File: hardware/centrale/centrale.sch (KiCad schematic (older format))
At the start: 36 parts, among them J1 MDCOG240128B6W, J2 Conn_BME280, J3 CONN_BME280_2, J4 RJ45, J5 Term_sel, Q1 BSS123, U1 MCP7940N-xSN, U2 TPS54228, U3 MCP2542FDxMF, Y1 32.768Khz

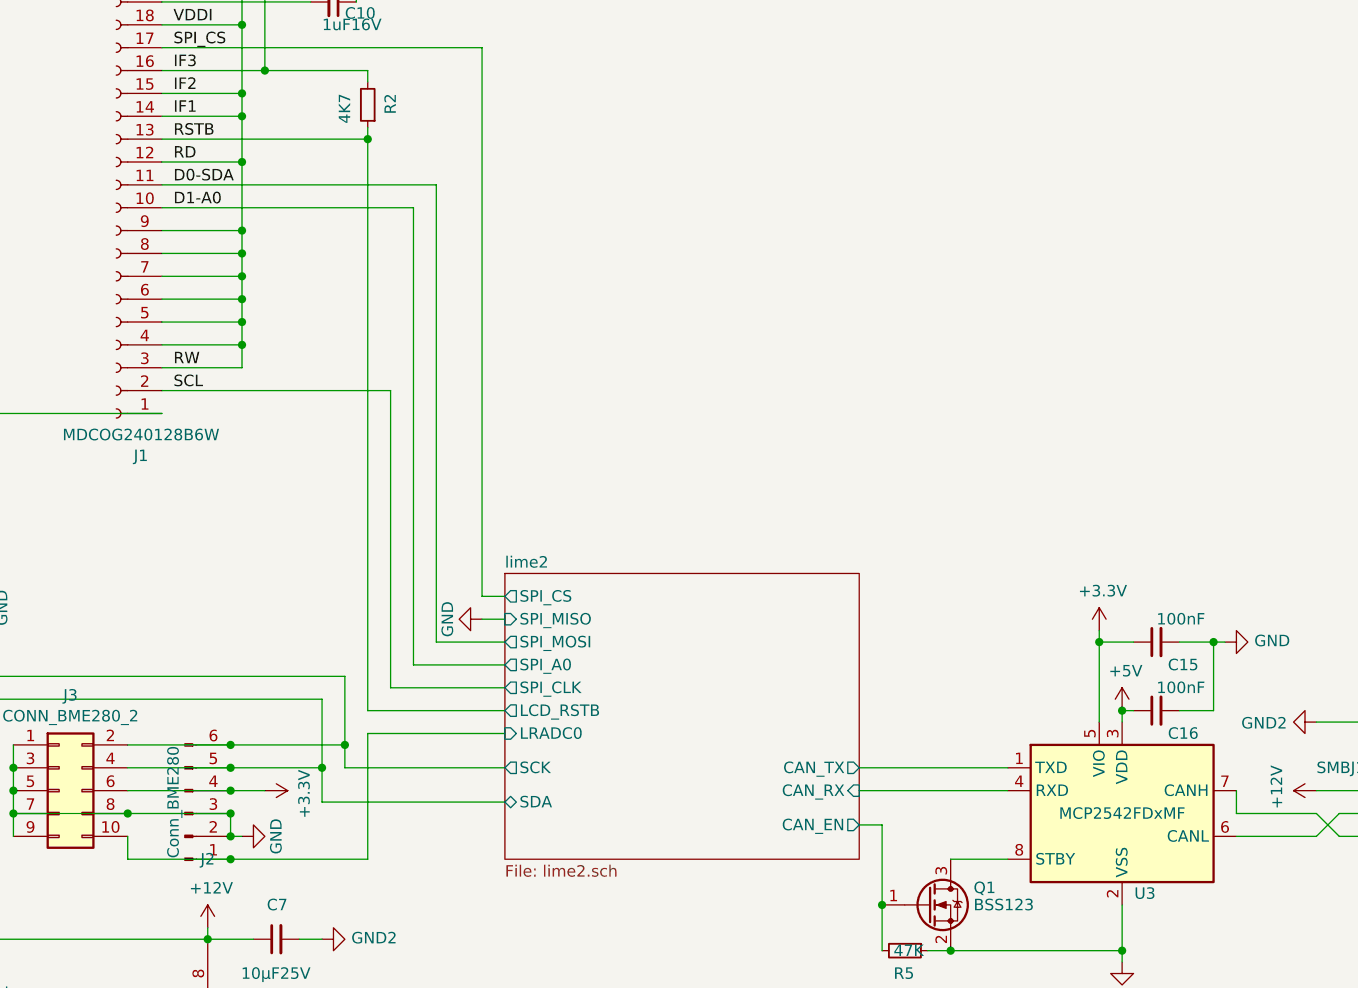
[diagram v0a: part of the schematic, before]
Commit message: Prepare for v2: fix display connector wiring, remplace the CAN transeiver with a pin-compatible one which is not out of stock, enlarge a bit the CPU cooling window.
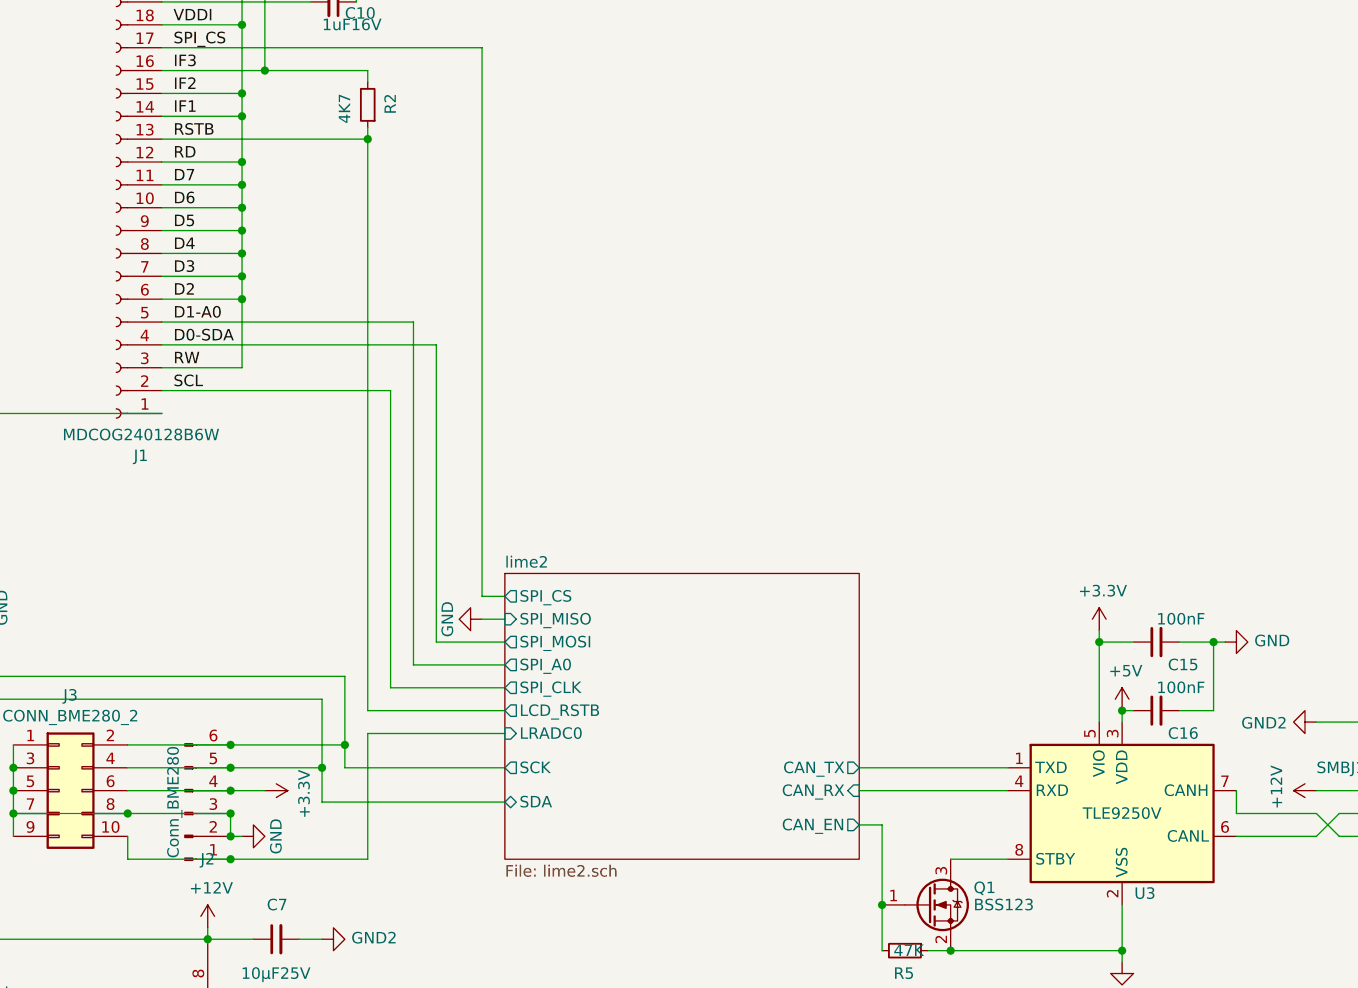
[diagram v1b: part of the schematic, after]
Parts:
- U3: value MCP2542FDxMF -> TLE9250V; P/N (none) -> TLE9250V
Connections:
- net +3V3: now also J1.10 (Pin_10), J1.11 (Pin_11); no longer J1.4 (Pin_4), J1.5 (Pin_5)
- net D0-SDA: now also J1.4 (Pin_4); no longer J1.11 (Pin_11)
- net D1-A0: now also J1.5 (Pin_5); no longer J1.10 (Pin_10)
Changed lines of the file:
@@
 P 7400 5200
 F 0 "U3" H 7500 4850 50  0000 C CNN
-F 1 "MCP2542FDxMF" H 7400 5200 50  0000 C CNN
+F 1 "TLE9250V" H 7400 5200 50  0000 C CNN
 F 2 "Package_SO:SOIC-8_3.9x4.9mm_P1.27mm" H 7400 4700 50  0001 C CIN
 F 3 "http://ww1.microchip.com/downloads/en/DeviceDoc/MCP2542FD-4FD-MCP2542WFD-4WFD-Data-Sheet20005514B.pdf" H 7400 5200 50  0001 C CNN
+F 4 "TLE9250V" H 7400 5200 50  0001 C CNN "P/N"
 	1    7400 5200
 	1    0    0    -1
@@
 Text Label 3250 2350 0    50   ~ 0
 RD
-Text Label 3250 2450 0    50   ~ 0
+Text Label 3250 3150 0    50   ~ 0
 D0-SDA
-Text Label 3250 2550 0    50   ~ 0
+Text Label 3250 3050 0    50   ~ 0
 D1-A0
 Text Label 3250 3250 0    50   ~ 0
@@
 Wire Wire Line
 	3200 3250 3550 3250
-Wire Wire Line
-	3550 3250 3550 3150
 Connection ~ 3550 2350
 Wire Wire Line
 	4700 4450 4400 4450
 Wire Wire Line
-	4400 4450 4400 2450
-Wire Wire Line
-	4400 2450 3200 2450
+	4400 4450 4400 3150
 Wire Wire Line
 	4700 4550 4300 4550
 Wire Wire Line
-	4300 4550 4300 2550
-Wire Wire Line
-	4300 2550 3200 2550
+	4300 4550 4300 3050
 Wire Wire Line
 	3200 3350 4200 3350
@@
 Connection ~ 3550 2650
 Wire Wire Line
-	3550 2650 3550 2350
+	3550 2650 3550 2550
 Wire Wire Line
 	3200 2750 3550 2750
@@
 Wire Wire Line
 	3550 2950 3550 2850
-Wire Wire Line
-	3200 3050 3550 3050
-Connection ~ 3550 3050
-Wire Wire Line
-	3550 3050 3550 2950
-Wire Wire Line
-	3200 3150 3550 3150
-Connection ~ 3550 3150
-Wire Wire Line
-	3550 3150 3550 3050
 $Comp
 L Device:C_Small C8
@@
 	2550 5200 2550 5300
 Connection ~ 3050 5200
+Wire Wire Line
+	3200 3150 4400 3150
+Wire Wire Line
+	3550 2950 3550 3250
+Wire Wire Line
+	3200 3050 4300 3050
+Wire Wire Line
+	3200 2550 3550 2550
+Connection ~ 3550 2550
+Wire Wire Line
+	3550 2550 3550 2450
+Wire Wire Line
+	3200 2450 3550 2450
+Connection ~ 3550 2450
+Wire Wire Line
+	3550 2450 3550 2350
+Text Label 3250 2950 0    50   ~ 0
+D2
+Text Label 3250 2850 0    50   ~ 0
+D3
+Text Label 3250 2750 0    50   ~ 0
+D4
+Text Label 3250 2650 0    50   ~ 0
+D5
+Text Label 3250 2550 0    50   ~ 0
+D6
+Text Label 3250 2450 0    50   ~ 0
+D7
 $EndSCHEMATC

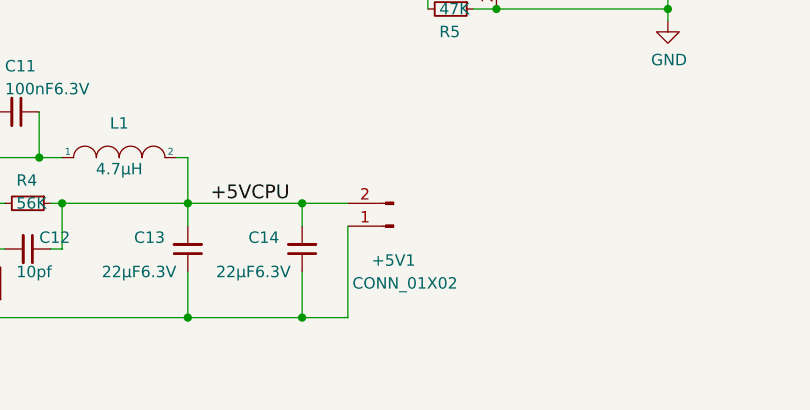
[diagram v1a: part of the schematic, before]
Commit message: Use a MC24356 connector for the CPU power supply. Other minor cleanups
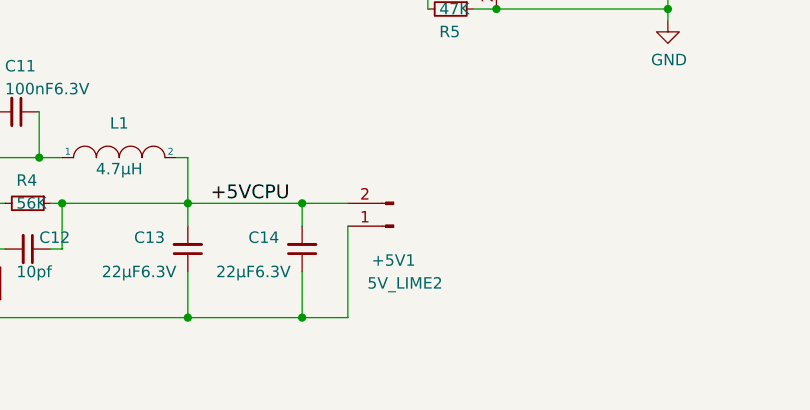
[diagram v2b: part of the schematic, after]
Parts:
- +5V1: value CONN_01X02 -> 5V_LIME2; footprint Connector_Wire:SolderWire-0.5sqmm_1x02_P4.8mm_D0.9mm_OD2.3mm -> local:MC24356; P/N (none) -> MC24356
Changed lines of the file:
@@
-$EndComp
-$Comp
-L Connector:Conn_01x02_Male +5V1
-U 1 1 60509668
-P 6200 6750
-F 0 "+5V1" H 6200 6900 50  0000 C CNN
-F 1 "CONN_01X02" H 6150 7000 50  0000 C CNN
-F 2 "Connector_Wire:SolderWire-0.5sqmm_1x02_P4.8mm_D0.9mm_OD2.3mm" H 6200 6750 50  0001 C CNN
-F 3 "" H 6200 6750 50  0000 C CNN
-	1    6200 6750
-	-1   0    0    1
 $EndComp
 $Comp
@@
 Text Label 3250 2450 0    50   ~ 0
 D7
+$Comp
+L Connector:Conn_01x02_Male +5V1
+U 1 1 60509668
+P 6200 6750
+F 0 "+5V1" H 6200 6900 50  0000 C CNN
+F 1 "5V_LIME2" H 6150 7000 50  0000 C CNN
+F 2 "local:MC24356" H 6200 6750 50  0001 C CNN
+F 3 "" H 6200 6750 50  0000 C CNN
+F 4 "MC24356" H 6200 6750 50  0001 C CNN "P/N"
+	1    6200 6750
+	-1   0    0    1
+$EndComp
 $EndSCHEMATC

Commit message: Change DC/DC output capacitors to 1210 size. Theses are better at 5V bias, hoping this will decrease the noise of the inductor.
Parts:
- C13, C14: footprint Capacitor_SMD:C_0805_2012Metric_Pad1.18x1.45mm_HandSolder -> Capacitor_SMD:C_1210_3225Metric_Pad1.33x2.70mm_HandSolder; P/N GRM21BR61E226ME44L -> C3225X5R1A226M230AA
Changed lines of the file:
@@
 F 0 "C14" H 5900 6800 50  0000 L CNN
 F 1 "22µF6.3V" H 5850 6950 50  0000 L CNN
-F 2 "Capacitor_SMD:C_0805_2012Metric_Pad1.18x1.45mm_HandSolder" H 5800 6850 50  0001 C CNN
+F 2 "Capacitor_SMD:C_1210_3225Metric_Pad1.33x2.70mm_HandSolder" H 5800 6850 50  0001 C CNN
 F 3 "" H 5800 6850 50  0000 C CNN
-F 4 "GRM21BR61E226ME44L " H 3000 7500 60  0001 C CNN "P/N"
+F 4 "C3225X5R1A226M230AA" H 3000 7500 60  0001 C CNN "P/N"
 	1    5800 6850
 	-1   0    0    1
@@
 F 0 "C13" H 5400 6800 50  0000 L CNN
 F 1 "22µF6.3V" H 5350 6950 50  0000 L CNN
-F 2 "Capacitor_SMD:C_0805_2012Metric_Pad1.18x1.45mm_HandSolder" H 5300 6850 50  0001 C CNN
+F 2 "Capacitor_SMD:C_1210_3225Metric_Pad1.33x2.70mm_HandSolder" H 5300 6850 50  0001 C CNN
 F 3 "" H 5300 6850 50  0000 C CNN
-F 4 "GRM21BR61E226ME44L " H 3000 7500 60  0001 C CNN "P/N"
+F 4 "C3225X5R1A226M230AA" H 3000 7500 60  0001 C CNN "P/N"
 	1    5300 6850
 	-1   0    0    1
